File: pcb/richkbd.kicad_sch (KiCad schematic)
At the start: 17 parts, among them J2 OLED, U1 ProMicro

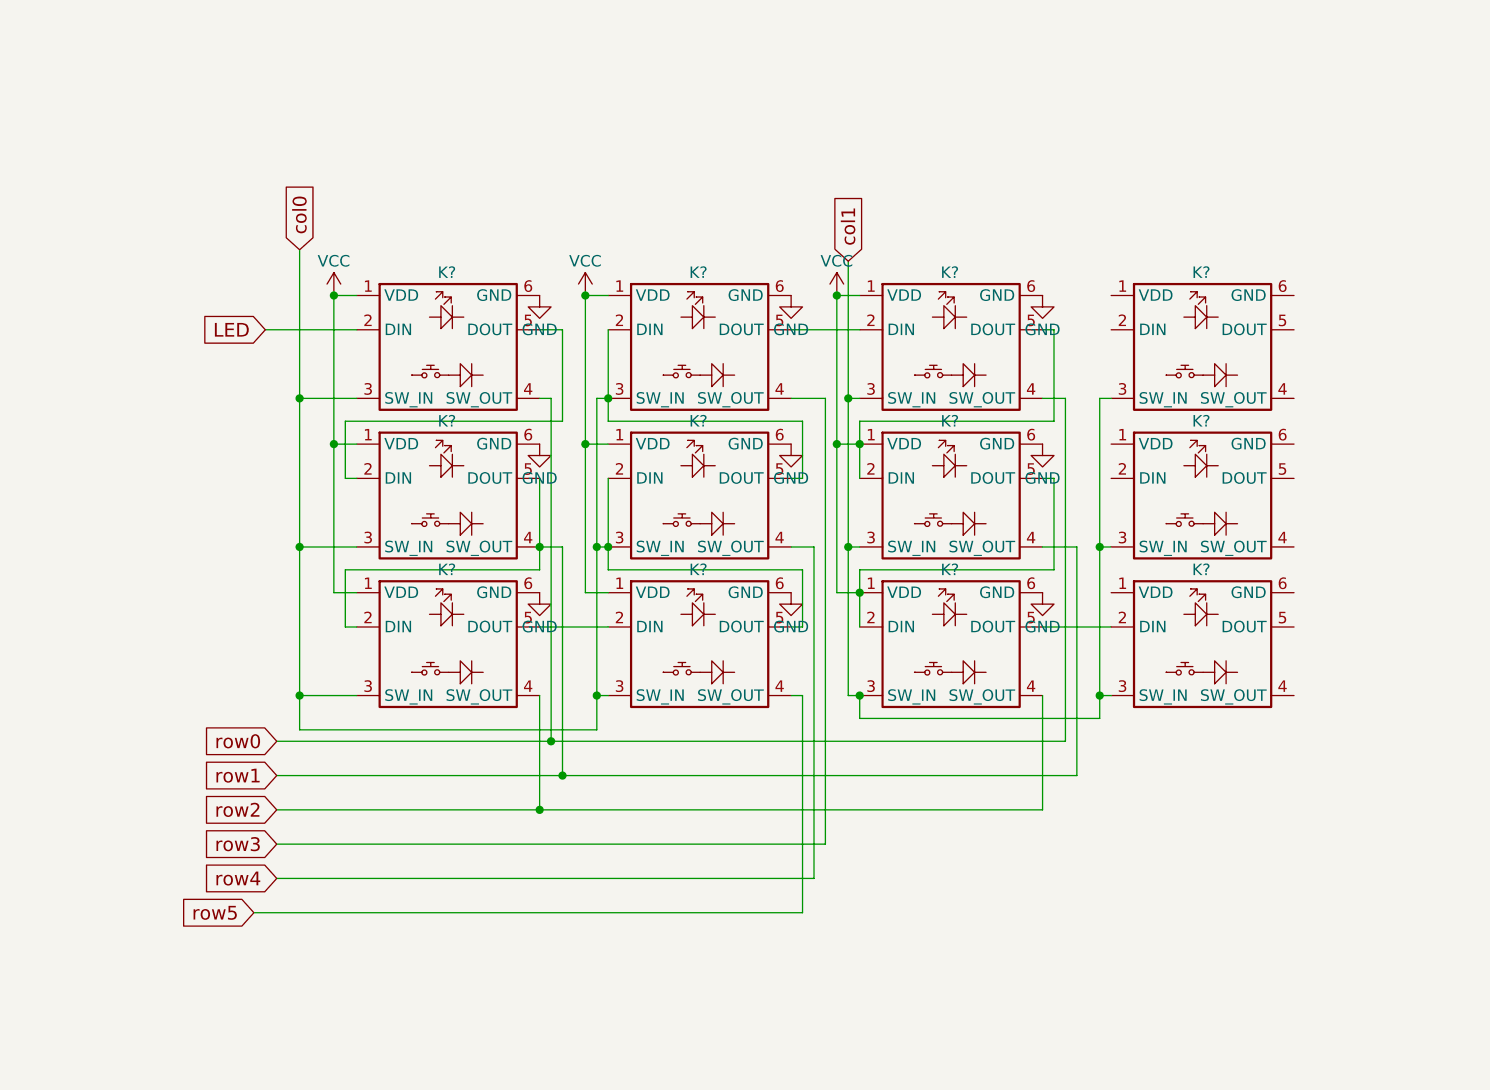
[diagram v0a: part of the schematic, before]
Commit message: Completed 2 columns of switches and improved symmetry
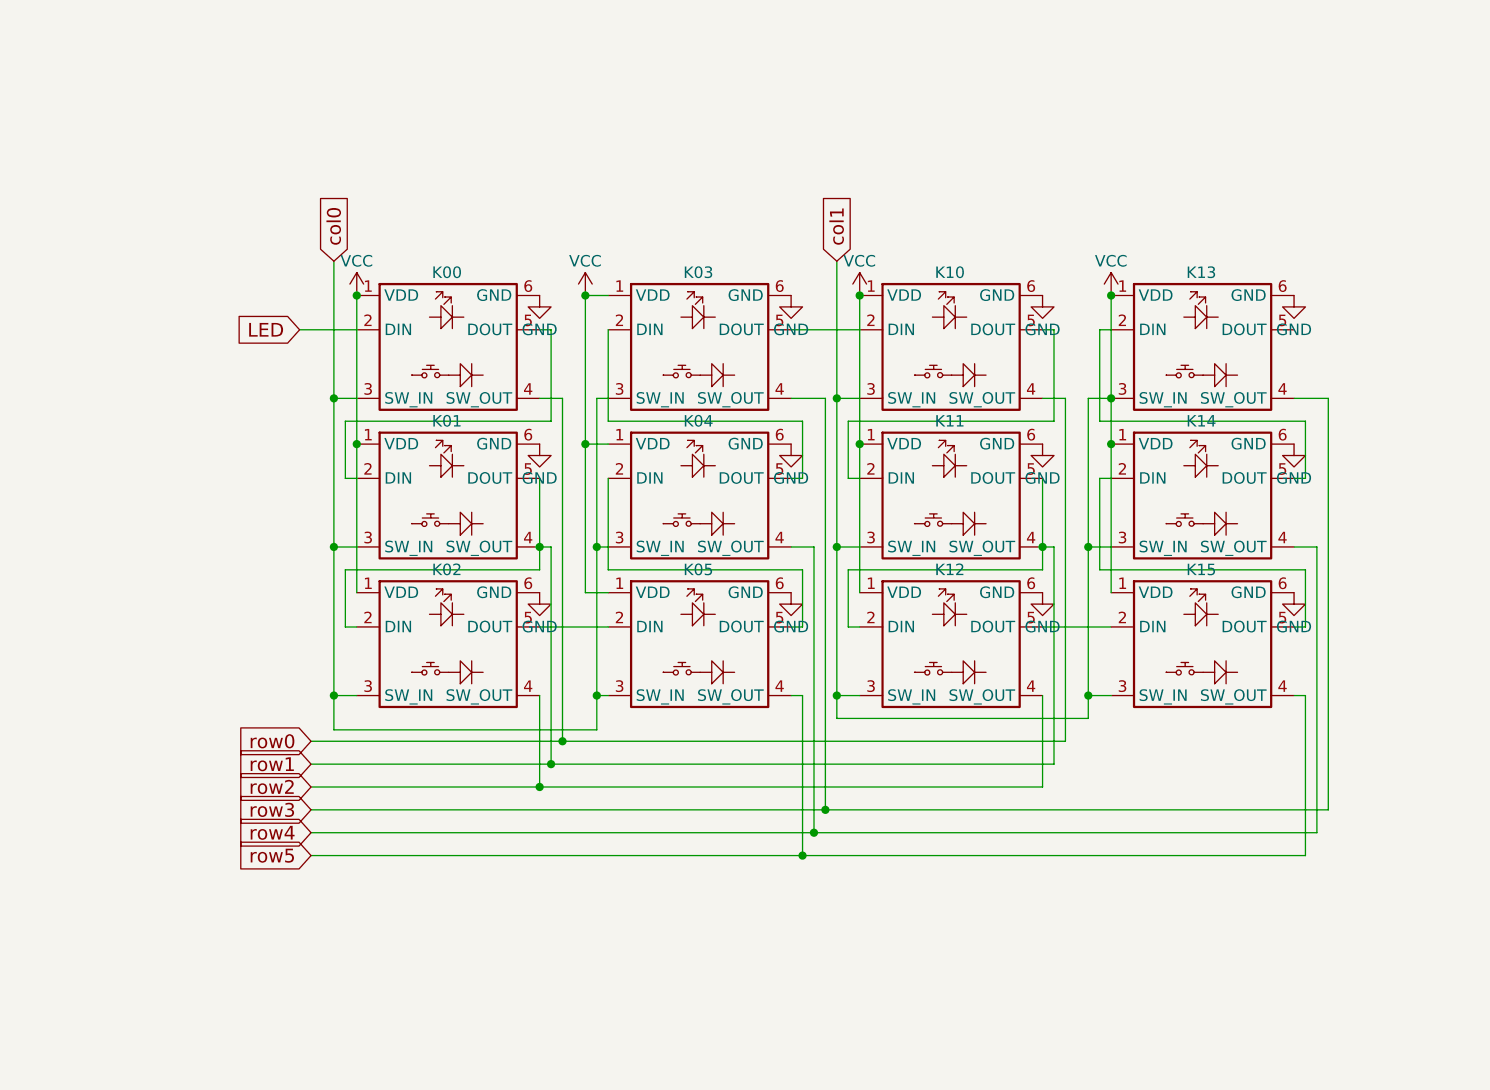
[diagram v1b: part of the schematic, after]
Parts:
- gave numbers to parts that had none: 12
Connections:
- net col1 is gone; now on net VCC: K10.3 (SW_IN), K11.3 (SW_IN), K12.3 (SW_IN), K13.3 (SW_IN), K14.3 (SW_IN), K15.3 (SW_IN), U1.19 (F5)
- net GND: now also K13.6 (GND), K14.6 (GND), K15.6 (GND)
- net VCC: now also K13.1 (VDD), K14.1 (VDD), K15.1 (VDD); no longer K10.5 (DOUT), K11.2 (DIN), K11.5 (DOUT), K12.2 (DIN)
- net col0: no longer K03.2 (DIN), K04.2 (DIN), K04.5 (DOUT), K05.5 (DOUT)
- net row1: now also K11.5 (DOUT), K12.2 (DIN)
- net row3: now also K13.4 (SW_OUT)
- net row4: now also K14.4 (SW_OUT)
- net row5: now also K15.4 (SW_OUT)
- net at K14.2 (DIN): now also K15.5 (DOUT)
- net at K14.5 (DOUT): now also K13.2 (DIN)
- new net: K10.5 (DOUT), K11.2 (DIN)
- new net: K04.2 (DIN), K05.5 (DOUT)
- new net: K03.2 (DIN), K04.5 (DOUT)

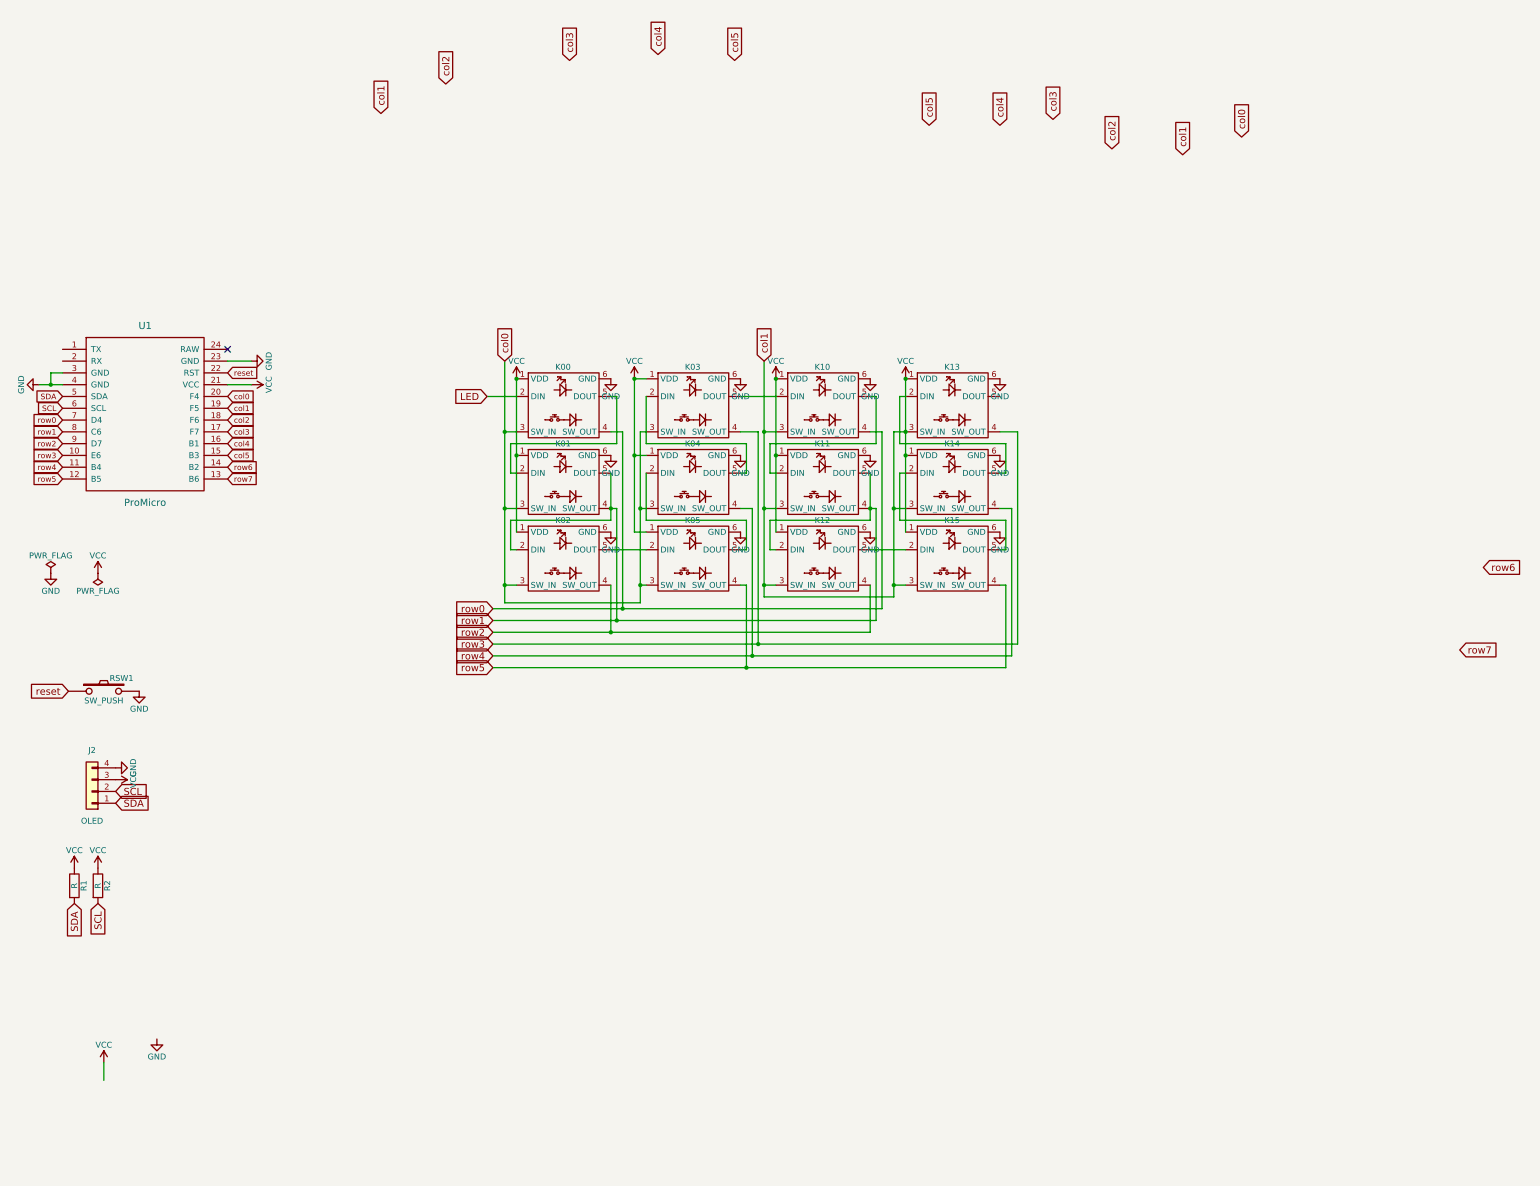
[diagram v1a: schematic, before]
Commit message: Completed schematic, but need to decide on rp2040 or not
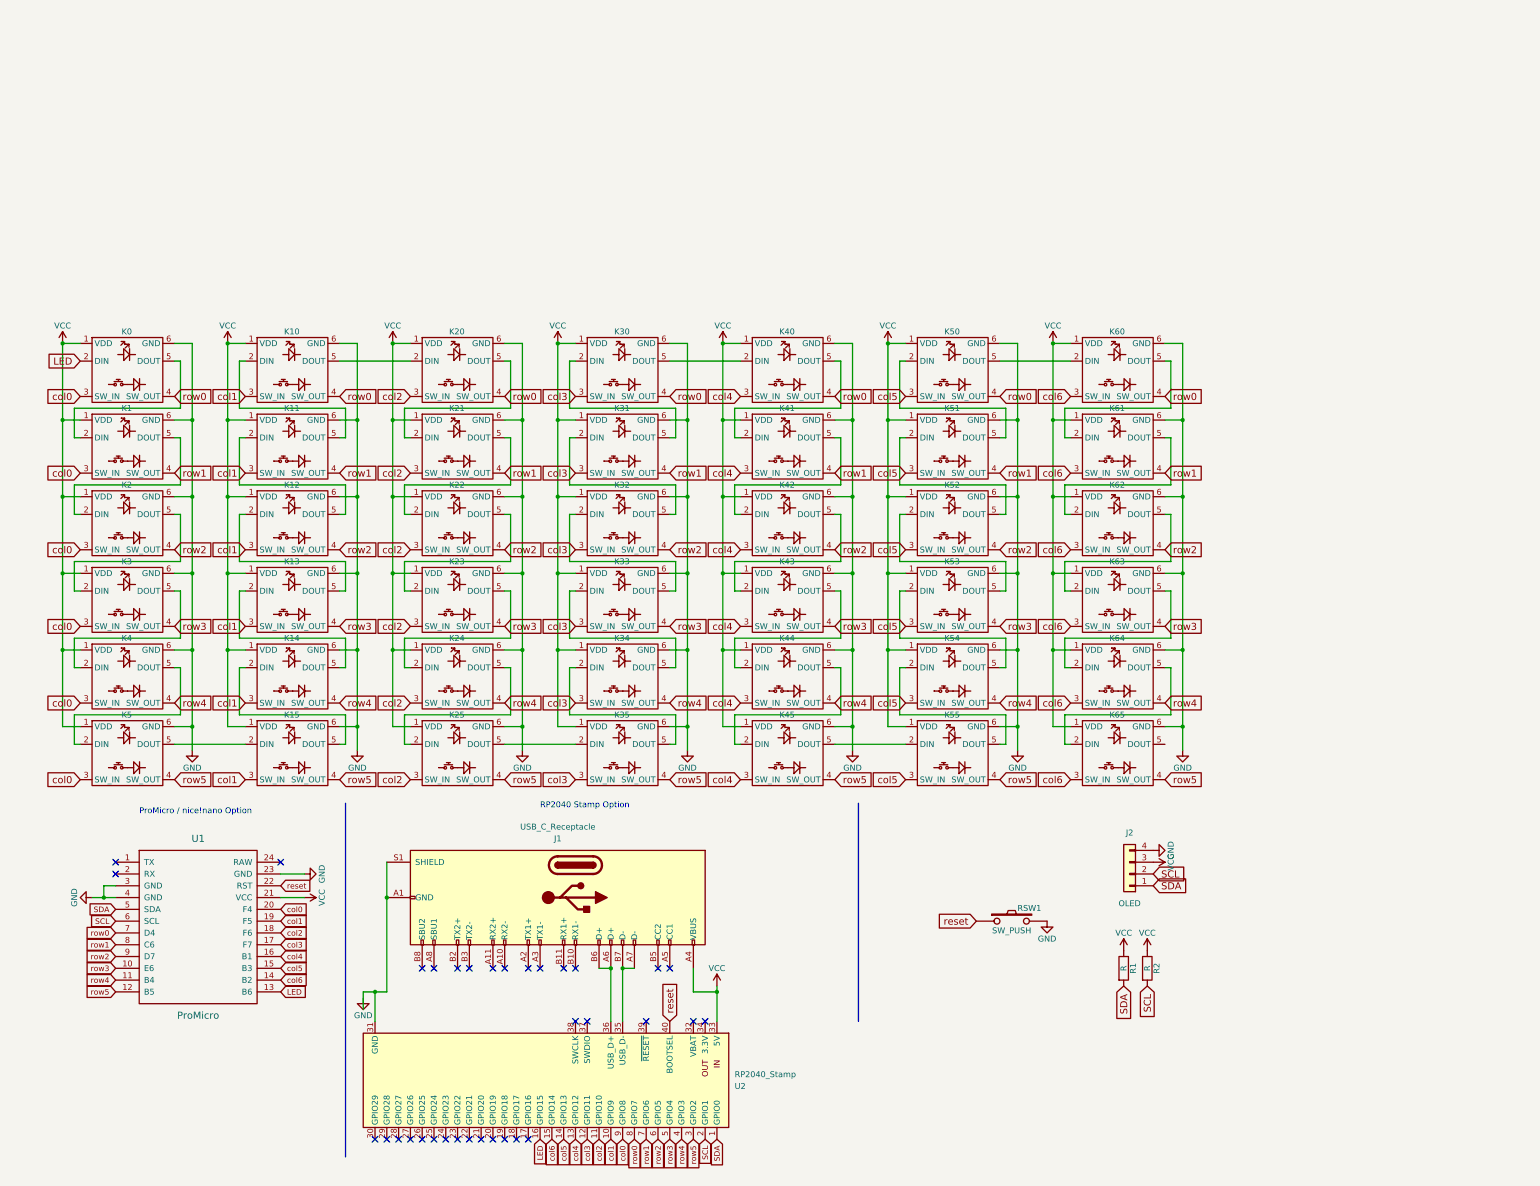
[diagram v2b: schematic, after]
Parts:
- removed K03, K04, K05: key-diode-led, nashlib:key_diode_led, symbol nashlib:key-diode-led
- added J1: USB_C_Receptacle, Connector_USB:USB_C_Receptacle_Amphenol_12401548E4-2A_CircularHoles, symbol Connector:USB_C_Receptacle
- added K20, K21, K22, K23, K24, K25, K3, K30, K31, K32, K33, K34, K35, K4, K40, K41, K42, K43, K44, K45, K5, K50, K51, K52, K53, K54, K55, K60, K61, K62, K63, K64, K65: key-diode-led, nashlib:key_diode_led, symbol nashlib:key-diode-led
- added U2: RP2040_Stamp, RP2040_Stamp:RP2040_Stamp_SMD, symbol RP2040_Stamp:RP2040_Stamp
- renumbered K00 to K0, K01 to K1, K02 to K2
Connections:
- net row7 is gone; now on net LED: U1.13 (B6)
- net GND: now also K20.6 (GND), K21.6 (GND), K22.6 (GND), K23.6 (GND), K24.6 (GND), K25.6 (GND), K3.6 (GND), K30.6 (GND), K31.6 (GND), K32.6 (GND), K33.6 (GND), K34.6 (GND), K35.6 (GND), K4.6 (GND), K40.6 (GND), K41.6 (GND), K42.6 (GND), K43.6 (GND), K44.6 (GND), K45.6 (GND), K5.6 (GND), K50.6 (GND), K51.6 (GND), K52.6 (GND), K53.6 (GND), K54.6 (GND), K55.6 (GND), K60.6 (GND), K61.6 (GND), K62.6 (GND), K63.6 (GND), K64.6 (GND), K65.6 (GND)
- net LED: now also U2.16 (GPIO15)
- net SCL: now also U2.2 (GPIO1)
- net SDA: now also U2.1 (GPIO0)
- net VCC: now also J1.A4 (VBUS), J1.A9 (VBUS), J1.B4 (VBUS), J1.B9 (VBUS), K20.1 (VDD), K21.1 (VDD), K22.1 (VDD), K23.1 (VDD), K24.1 (VDD), K25.1 (VDD), K3.1 (VDD), K30.1 (VDD), K31.1 (VDD), K32.1 (VDD), K33.1 (VDD), K34.1 (VDD), K35.1 (VDD), K4.1 (VDD), K40.1 (VDD), K41.1 (VDD), K42.1 (VDD), K43.1 (VDD), K44.1 (VDD), K45.1 (VDD), K5.1 (VDD), K50.1 (VDD), K51.1 (VDD), K52.1 (VDD), K53.1 (VDD), K54.1 (VDD), K55.1 (VDD), K60.1 (VDD), K61.1 (VDD), K62.1 (VDD), K63.1 (VDD), K64.1 (VDD), K65.1 (VDD), U2.33 (5V); no longer K10.3 (SW_IN), K11.3 (SW_IN), K12.3 (SW_IN), K13.3 (SW_IN), K14.3 (SW_IN), K15.3 (SW_IN), U1.19 (F5)
- net col0: now also K3.3 (SW_IN), K4.3 (SW_IN), K5.3 (SW_IN), U2.9 (GPIO8)
- net col2: now also K20.3 (SW_IN), K21.3 (SW_IN), K22.3 (SW_IN), K23.3 (SW_IN), K24.3 (SW_IN), K25.3 (SW_IN), U2.11 (GPIO10)
- net col3: now also K30.3 (SW_IN), K31.3 (SW_IN), K32.3 (SW_IN), K33.3 (SW_IN), K34.3 (SW_IN), K35.3 (SW_IN), U2.12 (GPIO11)
- net col4: now also K40.3 (SW_IN), K41.3 (SW_IN), K42.3 (SW_IN), K43.3 (SW_IN), K44.3 (SW_IN), K45.3 (SW_IN), U2.13 (GPIO12)
- net col5: now also K50.3 (SW_IN), K51.3 (SW_IN), K52.3 (SW_IN), K53.3 (SW_IN), K54.3 (SW_IN), K55.3 (SW_IN), U2.14 (GPIO13)
- net reset: now also U2.40 (BOOTSEL)
- net row0: now also K20.4 (SW_OUT), K30.4 (SW_OUT), K40.4 (SW_OUT), K50.4 (SW_OUT), K60.4 (SW_OUT), U2.8 (GPIO7)
- net row1: now also K21.4 (SW_OUT), K31.4 (SW_OUT), K41.4 (SW_OUT), K51.4 (SW_OUT), K61.4 (SW_OUT), U2.7 (GPIO6); no longer K1.5 (DOUT), K11.5 (DOUT), K12.2 (DIN), K2.2 (DIN)
- net row2: now also K22.4 (SW_OUT), K32.4 (SW_OUT), K42.4 (SW_OUT), K52.4 (SW_OUT), K62.4 (SW_OUT), U2.6 (GPIO5)
- net row3: now also K23.4 (SW_OUT), K3.4 (SW_OUT), K33.4 (SW_OUT), K43.4 (SW_OUT), K53.4 (SW_OUT), K63.4 (SW_OUT), U2.5 (GPIO4)
- net row4: now also K24.4 (SW_OUT), K34.4 (SW_OUT), K4.4 (SW_OUT), K44.4 (SW_OUT), K54.4 (SW_OUT), K64.4 (SW_OUT), U2.4 (GPIO3)
- net row5: now also K25.4 (SW_OUT), K35.4 (SW_OUT), K45.4 (SW_OUT), K5.4 (SW_OUT), K55.4 (SW_OUT), K65.4 (SW_OUT), U2.3 (GPIO2)
- net at K2.5 (DOUT): now also K3.2 (DIN)
- net at K12.5 (DOUT): now also K11.2 (DIN); no longer K15.2 (DIN)
- net at K10.2 (DIN): now also K11.5 (DOUT)
- net at K10.5 (DOUT): now also K20.2 (DIN); no longer K11.2 (DIN)
- net at K13.5 (DOUT): now also K12.2 (DIN)
- net row6 renamed col6
- net col6: now also K60.3 (SW_IN), K61.3 (SW_IN), K62.3 (SW_IN), K63.3 (SW_IN), K64.3 (SW_IN), K65.3 (SW_IN), U2.15 (GPIO14)
- new net: K61.5 (DOUT), K62.2 (DIN)
- new net: K62.5 (DOUT), K63.2 (DIN)
- new net: K1.5 (DOUT), K2.2 (DIN)
- new net: K31.2 (DIN), K32.5 (DOUT)
- new net: K30.2 (DIN), K31.5 (DOUT)
- new net: K54.2 (DIN), K55.5 (DOUT)
- new net: K53.2 (DIN), K54.5 (DOUT)
- new net: K30.5 (DOUT), K40.2 (DIN)
- new net: K40.5 (DOUT), K41.2 (DIN)
- new net: K22.5 (DOUT), K23.2 (DIN)
- new net: K23.5 (DOUT), K24.2 (DIN)
- new net: K50.2 (DIN), K51.5 (DOUT)
- new net: K50.5 (DOUT), K60.2 (DIN)
- new net: K63.5 (DOUT), K64.2 (DIN)
- new net: K64.5 (DOUT), K65.2 (DIN)
- new net: K32.2 (DIN), K33.5 (DOUT)
- new net: K52.2 (DIN), K53.5 (DOUT)
- new net: K51.2 (DIN), K52.5 (DOUT)
- new net: K24.5 (DOUT), K25.2 (DIN)
- new net: K25.5 (DOUT), K35.2 (DIN)
- new net: K34.2 (DIN), K35.5 (DOUT)
- new net: K33.2 (DIN), K34.5 (DOUT)
- new net: K20.5 (DOUT), K21.2 (DIN)
- new net: J1.A1 (GND), J1.A12 (GND), J1.B1 (GND), J1.B12 (GND), J1.S1 (SHIELD), U2.31 (GND)
- new net: J1.A7 (D-), J1.B7 (D-), U2.35 (USB_D-)
- new net: J1.A6 (D+), J1.B6 (D+), U2.36 (USB_D+)
- new net: K4.5 (DOUT), K5.2 (DIN)
- new net: K15.2 (DIN), K5.5 (DOUT)
- new net: K41.5 (DOUT), K42.2 (DIN)
- new net: K42.5 (DOUT), K43.2 (DIN)
- new net: K45.5 (DOUT), K55.2 (DIN)
- new net: K60.5 (DOUT), K61.2 (DIN)
- new net: K21.5 (DOUT), K22.2 (DIN)
- new net: K3.5 (DOUT), K4.2 (DIN)
- new net: K43.5 (DOUT), K44.2 (DIN)
- new net: K44.5 (DOUT), K45.2 (DIN)
- new net col1: K10.3 (SW_IN), K11.3 (SW_IN), K12.3 (SW_IN), K13.3 (SW_IN), K14.3 (SW_IN), K15.3 (SW_IN), U1.19 (F5), U2.10 (GPIO9)
- no-connect marks 1 -> 34
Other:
- note added: "ProMicro / nice!nano Option"
- note added: "RP2040 Stamp Option"
- company: foostan -> rvnash
- title: Corne Chocolate -> Rich Keyboard
- moved on the sheet: J2, R1, R2, RSW1, U1

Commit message: Start of board layout
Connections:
- net LED: now also U1.7 (D4); no longer U1.13 (B6)
- net col4: now also U1.8 (C6); no longer U1.16 (B1)
- net col5: now also U1.9 (D7); no longer U1.15 (B3)
- net col6: now also U1.10 (E6); no longer U1.14 (B2)
- net row0: now also U1.16 (B1), U2.3 (GPIO2); no longer U1.7 (D4), U2.8 (GPIO7)
- net row1: now also U1.14 (B2), U2.4 (GPIO3); no longer U1.8 (C6), U2.7 (GPIO6)
- net row2: now also U1.15 (B3), U2.5 (GPIO4); no longer U1.9 (D7), U2.6 (GPIO5)
- net row3: now also U1.11 (B4), U2.6 (GPIO5); no longer U1.10 (E6), U2.5 (GPIO4)
- net row4: now also U1.12 (B5), U2.7 (GPIO6); no longer U1.11 (B4), U2.4 (GPIO3)
- net row5: now also U1.13 (B6), U2.8 (GPIO7); no longer U1.12 (B5), U2.3 (GPIO2)
- no-connect marks 34 -> 35
